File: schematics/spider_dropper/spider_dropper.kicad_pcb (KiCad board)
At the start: 2 copper layers, 80 x 20 mm, 11 parts, among them J1 12V DC, J2 Sensor, J3 Motor, Q1 2N3904, Q2 TIP120, SW1 ZX40E10C01

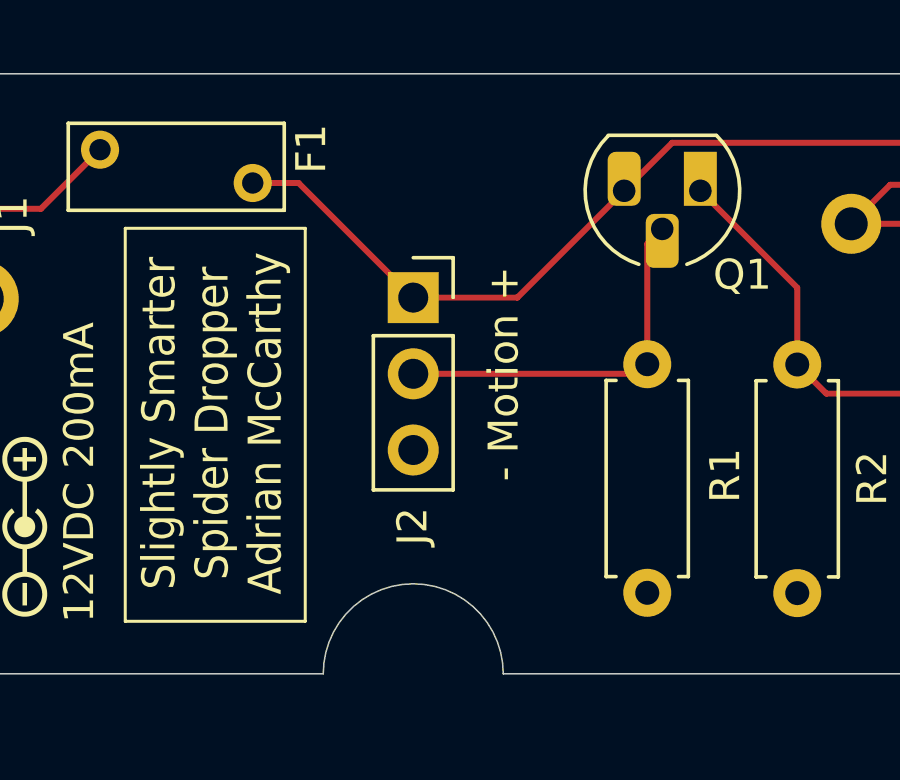
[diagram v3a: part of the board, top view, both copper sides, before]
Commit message: Changed PIR connector to JST XH, which is keyed and holds securely.
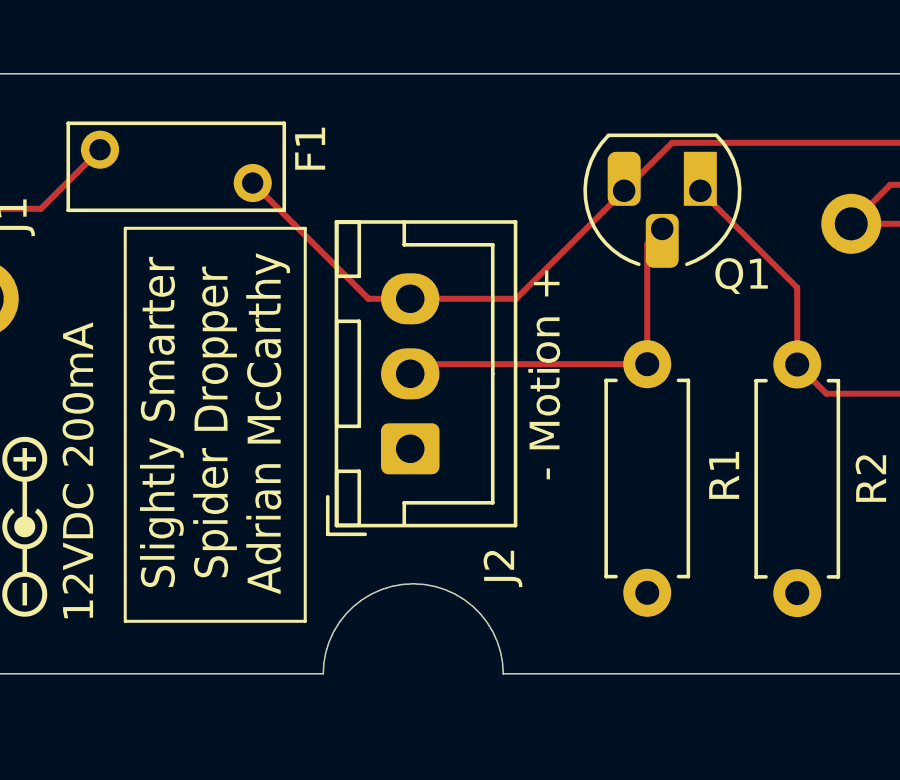
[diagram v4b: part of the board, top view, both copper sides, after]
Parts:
- J2: footprint Connector_PinSocket_2.54mm:PinSocket_1x03_P2.54mm_Vertical -> Connector_JST:JST_XH_B3B-XH-A_1x03_P2.50mm_Vertical
- moved J2 5.04 mm to (135.2, 110.8), turned to 90 degrees
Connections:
- J2 pad 1: Net-(D1-K) -> GND
- J2 pad 3: GND -> Net-(D1-K)

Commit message: Switched the JST XH footprint to one with hole for "boss".
The boss is for alignment and possibly additional support.  This
footprint is compatible with the connector that doesn't have a boss.
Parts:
- J2: footprint Connector_JST:JST_XH_B3B-XH-A_1x03_P2.50mm_Vertical -> Connector_JST:JST_XH_B3B-XH-AM_1x03_P2.50mm_Vertical
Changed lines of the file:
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@@
 		)
 	)
-	(footprint "Connector_JST:JST_XH_B3B-XH-A_1x03_P2.50mm_Vertical"
+	(footprint "Connector_JST:JST_XH_B3B-XH-AM_1x03_P2.50mm_Vertical"
 		(layer "F.Cu")
 		(at 135.2 110.8 90)
-		(descr "JST XH series connector, B3B-XH-A (http://www.jst-mfg.com/product/pdf/eng/eXH.pdf), generated with kicad-footprint-generator")
-		(tags "connector JST XH vertical")
+		(descr "JST XH series connector, B3B-XH-AM, with boss (http://www.jst-mfg.com/product/pdf/eng/eXH.pdf), generated with kicad-footprint-generator")
+		(tags "connector JST XH vertical boss")
 		(property "Reference" "J2"
-			(at -3.9 3 90)
+			(at 8.6 0 90)
 			(layer "F.SilkS")
 			(effects
@@
 			)
 		)
-		(property "Footprint" "Connector_JST:JST_XH_B3B-XH-A_1x03_P2.50mm_Vertical"
+		(property "Footprint" "Connector_JST:JST_XH_B3B-XH-AM_1x03_P2.50mm_Vertical"
 			(at 0 0 90)
 			(unlocked yes)
@@
 		(fp_line
 			(start -1.8 -0.2)
-			(end -1.8 2.75)
+			(end -1.8 1.14)
 			(stroke
 				(width 0.12)
@@
 		)
 		(fp_line
-			(start -1.8 2.75)
-			(end 2.5 2.75)
+			(start 2.5 2.75)
+			(end -0.74 2.75)
 			(stroke
 				(width 0.12)
@@
 				)
 			)
+		)
+		(pad "" np_thru_hole circle
+			(at -1.6 2 90)
+			(size 1.2 1.2)
+			(drill 1.2)
+			(layers "*.Cu" "*.Mask")
 		)
 		(pad "1" thru_hole roundrect
@@
 			(pintype "passive")
 		)
-		(model "${KICAD8_3DMODEL_DIR}/Connector_JST.3dshapes/JST_XH_B3B-XH-A_1x03_P2.50mm_Vertical.wrl"
+		(model "${KICAD8_3DMODEL_DIR}/Connector_JST.3dshapes/JST_XH_B3B-XH-AM_1x03_P2.50mm_Vertical.wrl"
 			(offset
 				(xyz 0 0 0)

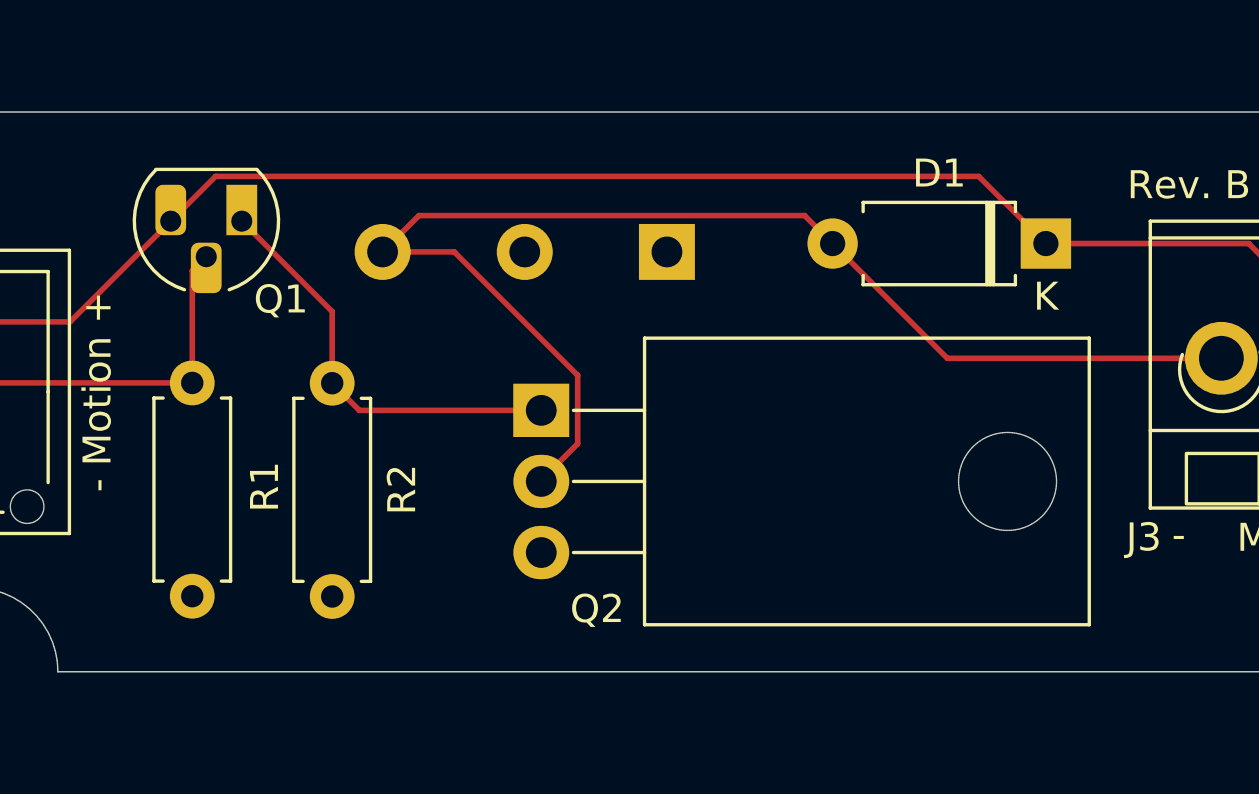
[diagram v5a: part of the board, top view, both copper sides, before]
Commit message: Tried to do circuit simulation in KiCad.  Not working yet.
The Spice models are from manufacturer OnSemi's website.
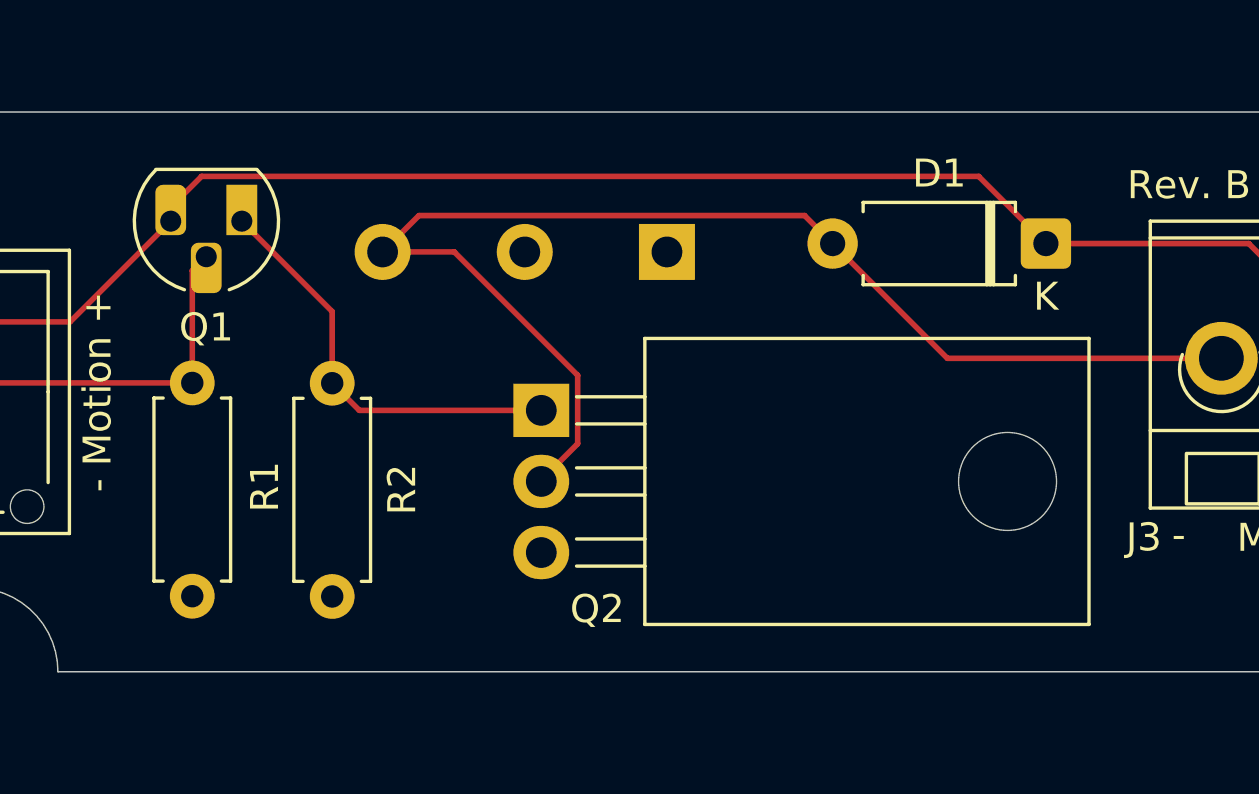
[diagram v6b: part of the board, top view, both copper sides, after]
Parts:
- Q1: footprint Package_TO_SOT_THT:TO-92_HandSolder -> Package_TO_SOT_THT:TO-92L_HandSolder

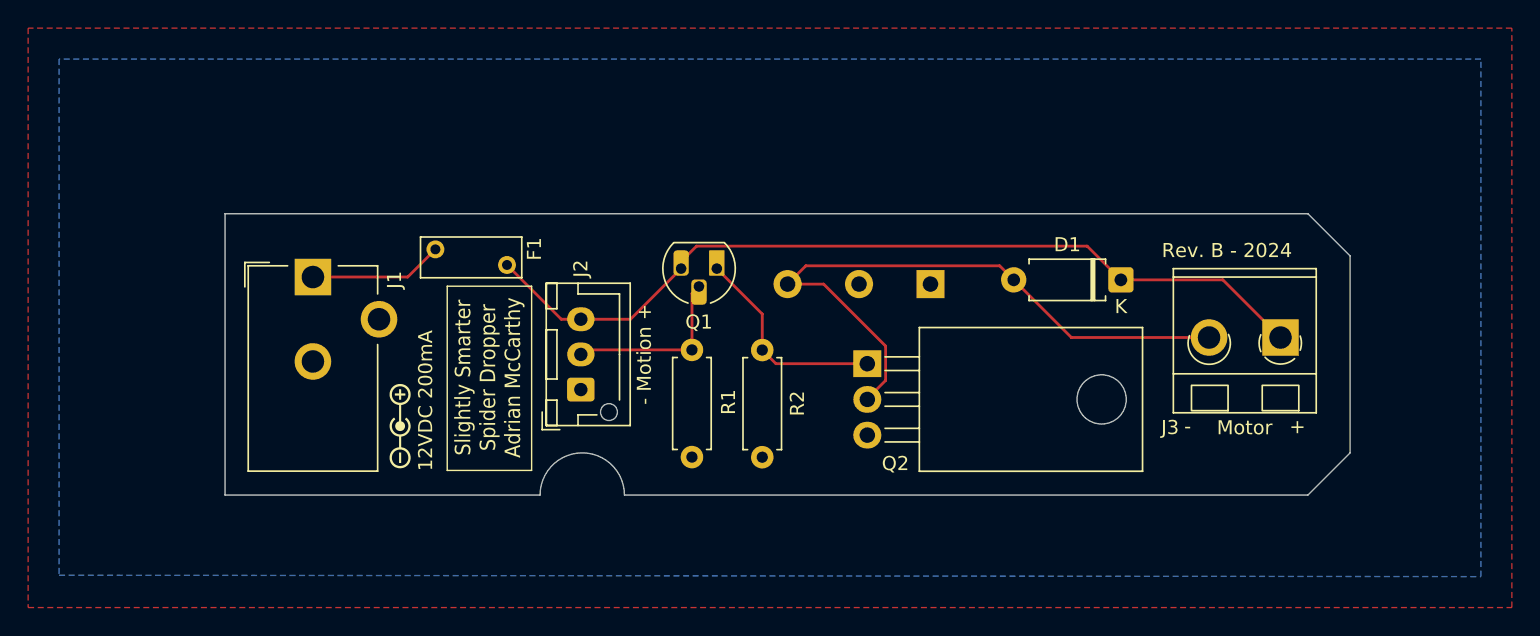
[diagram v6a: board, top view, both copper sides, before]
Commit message: Added current-limiting resistor to base of Q2.
With the thermal camera, I happened to notice that Q1 was heating up
more than I expected.  When on, it was passing almost 11mA.  Within
spec, but way more than necessary to turn on Q2.  Added a current
limited resistor to the base of Q2 dropped the current (and power)
through Q1 to less than 1mA.

Made additional layout tweaks to PCB and updated markings to Rev C.
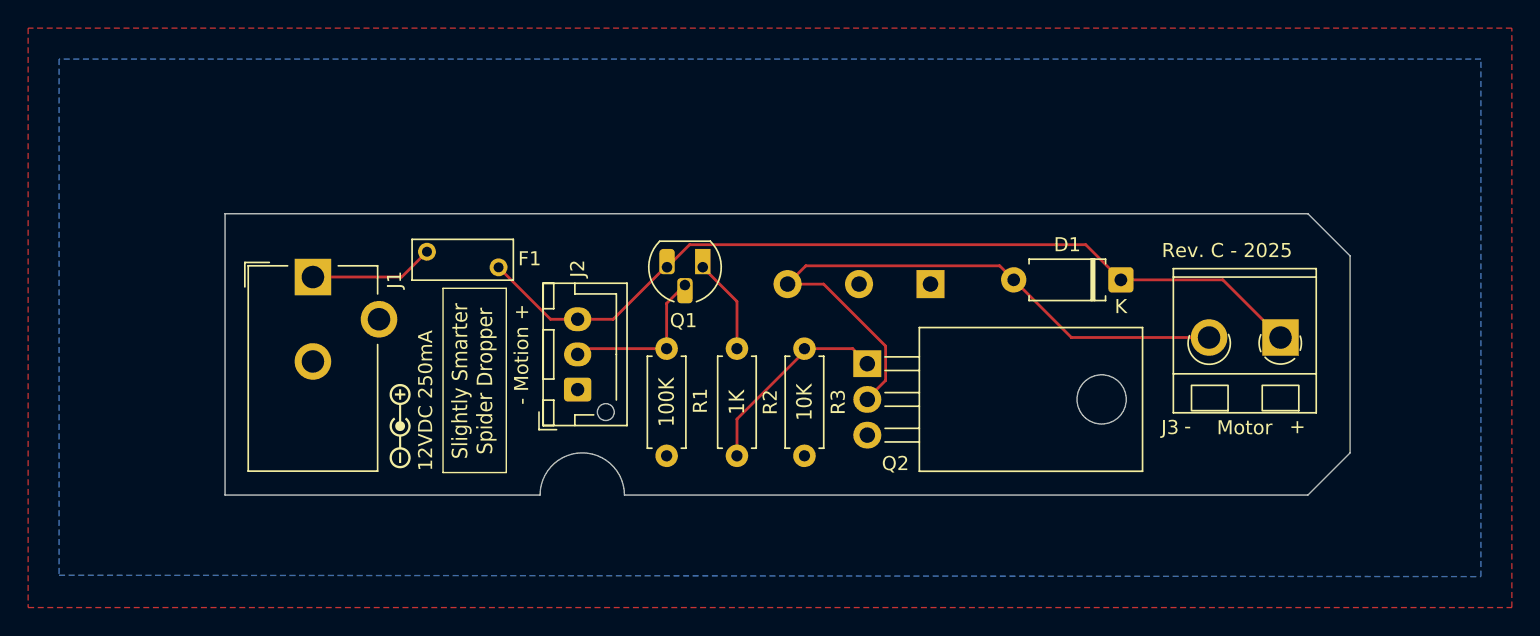
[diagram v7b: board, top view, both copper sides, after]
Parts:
- added R2: 1K, Resistor_THT:R_Axial_DIN0207_L6.3mm_D2.5mm_P7.62mm_Horizontal, F.Cu at (146.3, 107.9)
- F1: value PTC 90V 100mA -> PTC 90V 150mA
- moved R3 3.00 mm to (151.1, 107.9)
- moved R1 1.80 mm to (141.3, 107.9)
- moved Q1 1.00 mm to (143.9, 102.1)
- moved F1 0.62 mm to (124.3, 101.0)
- moved J2 0.22 mm to (135.0, 110.8)
- renumbered R2 to R3
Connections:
- Q2 pad 1: Net-(Q1-E) -> Net-(Q2-B)
- R3 pad 1: Net-(Q1-E) -> Net-(Q2-B)
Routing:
- net Net-(Q2-B): track 0.00 -> 14.5 mm
- net Net-(Q1-E): track 15.0 -> 6.80 mm
- net Net-(J2-Pin_2): track 12.7 -> 11.6 mm
- net +12V: track 9.53 -> 8.86 mm
- net Net-(D1-K): track 61.8 -> 62.4 mm
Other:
- board text added: "100K"
- board text added: "10K"
- board text added: "12VDC 250mA"
- board text added: "1K"
- board text added: "Rev. C - 2025"
- board text added: "Slightly Smarter Spider Dropper"
- board text removed: "12VDC 200mA"
- board text removed: "Rev. B - 2024"
- board text removed: "Slightly Smarter Spider Dropper Adrian McCarthy"

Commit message: Redesign of slightly smarter PCB.
Simplified by using a MOSFET, which requires fewer parts and runs the
motor more efficiently.  Since I'm also working on a re-do of the
printed parts, I went ahead and changed the layout and mounting options
for the board.  That makes the new PCB incompatible with the old
mechanical design.
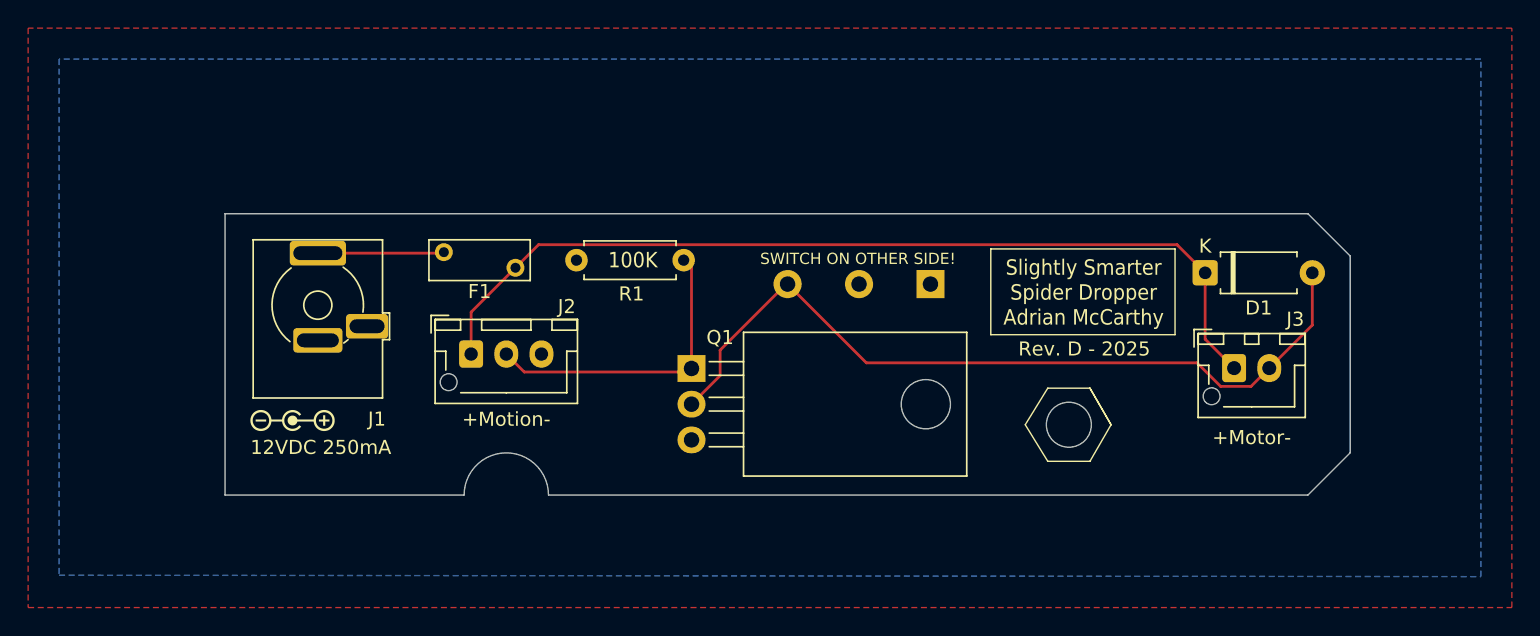
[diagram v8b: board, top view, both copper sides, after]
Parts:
- removed Q2: TIP120, Package_TO_SOT_THT:TO-220-3_Horizontal_TabDown
- removed R2: 1K, Resistor_THT:R_Axial_DIN0207_L6.3mm_D2.5mm_P7.62mm_Horizontal
- removed R3: 10K, Resistor_THT:R_Axial_DIN0207_L6.3mm_D2.5mm_P7.62mm_Horizontal
- added H1: M3, MountingHole:MountingHole_3.2mm_M3, B.Cu at (169.9, 113.3)
- F1: value PTC 90V 150mA -> PTC 250mA
- J1: footprint Connector_BarrelJack:BarrelJack_CUI_PJ-102AH_Horizontal -> aid_Connector:BarrelJack_SameSky(CUI)_PJ-044AH
- J2: value Sensor -> JST_XH_3
- J3: value Motor -> JST_XH_2; footprint aid_Connector:CUI_TB007-508_01x02_THT_Screw_Terminal_Block -> Connector_JST:JST_XH_B2B-XH-AM_1x02_P2.50mm_Vertical
- Q1: value 2N3904 -> IRLZ34N; footprint Package_TO_SOT_THT:TO-92L_HandSolder -> Package_TO_SOT_THT:TO-220-3_Horizontal_TabDown
- SW1: value ZX40E10C01 -> ZX40E20C01
- moved J2 7.98 mm to (127.4, 108.3), turned to 0 degrees
- moved G1 7.66 mm to (114.7, 113.0), turned to 0 degrees
- moved Q1 7.24 mm to (143.1, 109.3), turned to -90 degrees
- moved R1 6.41 mm to (142.5, 101.6), turned to 180 degrees
- moved D1 6.01 mm to (179.6, 102.5), turned to 0 degrees
- moved J3 3.95 mm to (181.7, 109.3), turned to 0 degrees
- moved J1 2.03 mm to (116.5, 104.8)
- moved F1 1.20 mm to (125.5, 101.0)
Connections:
- D1 pad 1: Net-(D1-K) -> /MOTOR+
- D1 pad 2: Net-(D1-A) -> /MOTOR-
- F1 pad 2: Net-(D1-K) -> /MOTOR+
- J2 pad 1: GND -> /MOTOR+
- J2 pad 2: Net-(J2-Pin_2) -> /MOTION
- J2 pad 3: Net-(D1-K) -> GND
- J3 pad 1: Net-(D1-K) -> /MOTOR+
- J3 pad 2: Net-(D1-A) -> /MOTOR-
- Q1 pad 1: Net-(Q1-E) -> /MOTION
- Q1 pad 2: Net-(J2-Pin_2) -> /MOTOR-
- Q1 pad 3: Net-(D1-K) -> GND
- R1 pad 1: Net-(J2-Pin_2) -> /MOTION
- SW1 pad 3: Net-(D1-A) -> /MOTOR-
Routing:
- net /MOTOR+: track 0.00 -> 65.6 mm
- net Net-(D1-K): track 62.4 -> 0.00 mm
- net /MOTOR-: track 0.00 -> 57.2 mm
- net Net-(D1-A): track 45.7 -> 0.00 mm
- net /MOTION: track 0.00 -> 21.7 mm
- net Net-(Q2-B): track 14.5 -> 0.00 mm
- net Net-(J2-Pin_2): track 11.6 -> 0.00 mm
- net Net-(Q1-E): track 6.80 -> 0.00 mm
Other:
- outline, holes or cut-outs redrawn
- board text added: "+Motion-"
- board text added: "+Motor-"
- board text added: "M3"
- board text added: "Rev. D - 2025"
- board text added: "SWITCH ON OTHER SIDE!"
- board text added: "Slightly Smarter Spider Dropper Adrian McCarthy"
- board text removed: "+"
- board text removed: "-"
- board text removed: "- Motion +"
- board text removed: "10K"
- board text removed: "1K"
- board text removed: "Motor"
- board text removed: "Rev. C - 2025"
- board text removed: "Slightly Smarter Spider Dropper"
